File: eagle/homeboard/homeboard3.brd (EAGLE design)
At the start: 100 x 80 mm, 81 parts, among them IC1 XCF02S, IC2 25LC080SN, Q5 BC848SMD, Q6 BC848SMD, Q7 BC848SMD, Q8 BC848SMD, T1 BSS138, T2 BC848, T3 BSS138, U1 XC3S400TQ144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

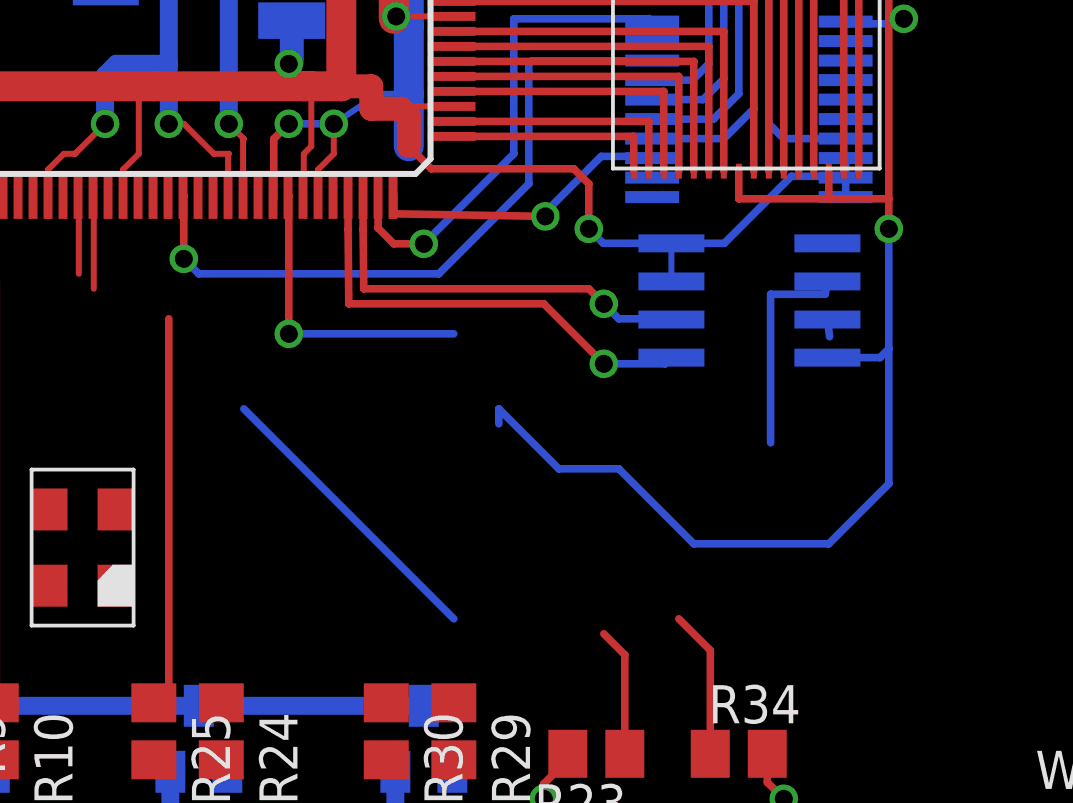
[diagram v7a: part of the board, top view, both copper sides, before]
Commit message: wired up prog and flash
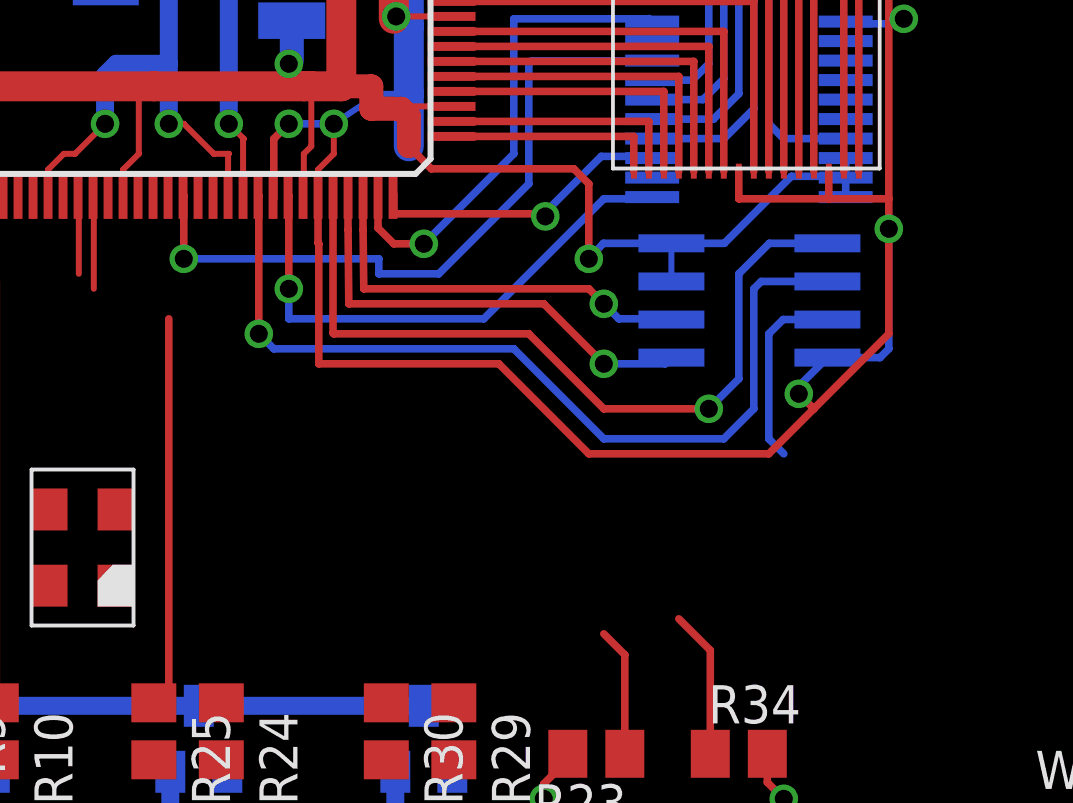
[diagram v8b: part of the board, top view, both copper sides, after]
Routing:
- net SPI_SEL0: track 0.00 -> 26.5 mm, vias 0 -> 1
- net GND: track 271.5 -> 284.2 mm, vias 20 -> 21
- net MISO: track 17.1 -> 29.6 mm, vias 0 -> 1
- net PROM_DO: track 10.2 -> 17.9 mm
- net N$49: track 0.58 -> 6.36 mm
- net VCC: track 221.5 -> 222.6 mm
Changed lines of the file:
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@@
 <wire x1="51" y1="16.1" x2="50.35" y2="16.75" width="0.254" layer="16"/>
 <wire x1="50.35" y1="16.75" x2="53.65" y2="16.75" width="0.254" layer="16"/>
-<wire x1="59.5" y1="33.5" x2="59.5" y2="29" width="0.254" layer="16"/>
-<wire x1="59.5" y1="29" x2="57.5" y2="27" width="0.254" layer="16"/>
-<wire x1="57.5" y1="27" x2="53" y2="27" width="0.254" layer="16"/>
-<wire x1="53" y1="27" x2="50.5" y2="29.5" width="0.254" layer="16"/>
-<wire x1="50.5" y1="29.5" x2="48.5" y2="29.5" width="0.254" layer="16"/>
-<wire x1="48.5" y1="29.5" x2="46.5" y2="31.5" width="0.254" layer="16"/>
-<wire x1="46.5" y1="31.5" x2="46.5" y2="31" width="0.254" layer="16"/>
+<wire x1="40.475" y1="38.63" x2="40.475" y2="37.025" width="0.254" layer="1"/>
+<wire x1="40.475" y1="37.025" x2="40.5" y2="37" width="0.254" layer="1"/>
+<wire x1="40.5" y1="37" x2="40.5" y2="33" width="0.254" layer="1"/>
+<wire x1="40.5" y1="33" x2="46.5" y2="33" width="0.254" layer="1"/>
+<wire x1="46.5" y1="33" x2="49.5" y2="30" width="0.254" layer="1"/>
+<via x="56.5" y="32" extent="1-16" drill="0.6" shape="square"/>
+<wire x1="56.5" y1="32" x2="56.5" y2="32.252359375" width="0.254" layer="16"/>
+<wire x1="56.5" y1="32.252359375" x2="57.453553125" y2="33.2059125" width="0.254" layer="16"/>
+<wire x1="49.5" y1="30" x2="55.5" y2="30" width="0.254" layer="1"/>
+<wire x1="55.5" y1="30" x2="57" y2="31.5" width="0.254" layer="1"/>
+<wire x1="57" y1="31.5" x2="59.5" y2="34" width="0.254" layer="1"/>
+<wire x1="59.5" y1="34" x2="59.5" y2="37.5" width="0.254" layer="1"/>
+<wire x1="56.5" y1="32" x2="57" y2="31.5" width="0.254" layer="1"/>
 <wire x1="96.05" y1="71" x2="95.55" y2="76" width="0" layer="19" extent="1-1"/>
 <wire x1="96.55" y1="67.5" x2="96.05" y2="71" width="0" layer="19" extent="1-1"/>
@@
 <wire x1="38.975" y1="38.63" x2="39" y2="38.5" width="0" layer="19" extent="1-1"/>
 <wire x1="29.475" y1="38.63" x2="28" y2="38.655" width="0" layer="19" extent="1-1"/>
-<wire x1="46.5" y1="31.5" x2="43.5" y2="40.25" width="0" layer="19" extent="16-16"/>
-<wire x1="53.65" y1="16.75" x2="53" y2="27" width="0" layer="19" extent="16-16"/>
+<wire x1="33.725" y1="28.145" x2="40.5" y2="33" width="0" layer="19" extent="1-1"/>
+<wire x1="50.35" y1="16.75" x2="49.5" y2="30" width="0" layer="19" extent="1-16"/>
 <wire x1="46.335" y1="7.5" x2="46.5" y2="7.5" width="0" layer="19" extent="1-1"/>
 <wire x1="19.665" y1="7.5" x2="19.5" y2="7.5" width="0" layer="19" extent="1-1"/>
 <wire x1="21.5" y1="4.93" x2="19.5" y2="5" width="0" layer="19" extent="1-1"/>
-<wire x1="33.725" y1="28.145" x2="29.475" y2="38.63" width="0" layer="19" extent="1-1"/>
-<wire x1="70.77" y1="21.75" x2="59.5" y2="29" width="0" layer="19" extent="16-16"/>
+<wire x1="70.77" y1="21.75" x2="59.2059125" y2="33.2059125" width="0" layer="19" extent="16-16"/>
 <wire x1="70.77" y1="18" x2="70.77" y2="21.75" width="0" layer="19" extent="1-1"/>
 <wire x1="17.3716" y1="78.27" x2="34.9778" y2="77" width="0" layer="19" extent="1-1"/>
@@
 <wire x1="58.043396875" y1="39.206603125" x2="58" y2="39.25" width="0.254" layer="16"/>
 <wire x1="52.253553125" y1="37.0159125" x2="49.9840875" y2="37.0159125" width="0.254" layer="16"/>
-<wire x1="49.9840875" y1="37.0159125" x2="49.5" y2="37.5" width="0.254" layer="16"/>
-<via x="49.5" y="37.5" extent="1-16" drill="0.6" shape="square"/>
-<wire x1="49.5" y1="37.5" x2="49.5" y2="39" width="0.254" layer="1"/>
+<wire x1="49.9840875" y1="37.0159125" x2="49.5" y2="36.5" width="0.254" layer="16"/>
+<via x="49.5" y="36.5" extent="1-16" drill="0.6" shape="square"/>
+<wire x1="49.5" y1="36.5" x2="49.5" y2="39" width="0.254" layer="1"/>
 <wire x1="49.5" y1="39" x2="49" y2="39.5" width="0.254" layer="1"/>
 <wire x1="49" y1="39.5" x2="44.25" y2="39.5" width="0.254" layer="1"/>
@@
 <wire x1="47.5" y1="43" x2="47.5" y2="39" width="0.254" layer="16"/>
 <wire x1="47.5" y1="39" x2="44.5" y2="36" width="0.254" layer="16"/>
-<wire x1="44.5" y1="36" x2="36.5" y2="36" width="0.254" layer="16"/>
-<wire x1="36.5" y1="36" x2="36" y2="36.5" width="0.254" layer="16"/>
+<wire x1="44.5" y1="36" x2="42.5" y2="36" width="0.254" layer="16"/>
+<wire x1="42.5" y1="36" x2="42.5" y2="36.5" width="0.254" layer="16"/>
+<wire x1="42.5" y1="36.5" x2="36" y2="36.5" width="0.254" layer="16"/>
 </signal>
 <signal name="N$39">
@@
 <wire x1="51.612590625" y1="39.856603125" x2="51.55498125" y2="39.9142125" width="0.254" layer="16"/>
 <wire x1="43" y1="38.655" x2="43" y2="38" width="0.254" layer="1"/>
-<wire x1="43" y1="38" x2="48.05025" y2="37.9142125" width="0.254" layer="1"/>
 <wire x1="51.55498125" y1="39.9142125" x2="49.9142125" y2="39.9142125" width="0.254" layer="16"/>
 <wire x1="49.9142125" y1="39.9142125" x2="48" y2="38" width="0.254" layer="16"/>
 <wire x1="48" y1="38" x2="48" y2="37.9644625" width="0.254" layer="16"/>
 <wire x1="48" y1="37.9644625" x2="48.05025" y2="37.9142125" width="0.254" layer="16"/>
+<wire x1="43" y1="38" x2="48" y2="38" width="0.254" layer="1"/>
+<wire x1="48.05025" y1="37.9142125" x2="48.05025" y2="37.94975" width="0.254" layer="1"/>
+<wire x1="48.05025" y1="37.94975" x2="48" y2="38" width="0.254" layer="1"/>
 </signal>
 <signal name="N$38">
@@
 <contactref element="U1" pad="P65"/>
 <wire x1="51.612590625" y1="38.556603125" x2="51.555984375" y2="38.5" width="0.254" layer="16"/>
-<via x="39.5" y="34" extent="1-16" drill="0.6" shape="square"/>
-<wire x1="39.5" y1="34" x2="39.5" y2="38.605" width="0.254" layer="1"/>
+<via x="39.5" y="35.5" extent="1-16" drill="0.6" shape="square"/>
+<wire x1="39.5" y1="35.5" x2="39.5" y2="38.605" width="0.254" layer="1"/>
 <wire x1="39.5" y1="38.605" x2="39.475" y2="38.63" width="0.254" layer="1"/>
-<wire x1="45" y1="34" x2="39.5" y2="34" width="0.254" layer="16"/>
-<wire x1="45" y1="34" x2="51.555984375" y2="38.5" width="0" layer="19" extent="16-16"/>
+<wire x1="51.555984375" y1="38.5" x2="50" y2="38.5" width="0.254" layer="16"/>
+<wire x1="50" y1="38.5" x2="46" y2="34.5" width="0.254" layer="16"/>
+<wire x1="46" y1="34.5" x2="39.5" y2="34.5" width="0.254" layer="16"/>
+<wire x1="39.5" y1="34.5" x2="39.5" y2="35.5" width="0.254" layer="16"/>
 </signal>
 <signal name="VCCINT">
@@
 <contactref element="IC2" pad="2"/>
 <contactref element="U$3" pad="11"/>
-<wire x1="57.453553125" y1="35.7459125" x2="57.381446875" y2="35.31801875" width="0.254" layer="16"/>
-<wire x1="57.381446875" y1="35.31801875" x2="55.560659375" y2="35.31801875" width="0.254" layer="16"/>
-<wire x1="55.560659375" y1="35.31801875" x2="55.560659375" y2="30.368271875" width="0.254" layer="16"/>
-<wire x1="45" y1="24.5" x2="38" y2="31.5" width="0.254" layer="16"/>
 <contactref element="U1" pad="P63"/>
+<wire x1="54" y1="30.5" x2="50" y2="30.5" width="0.254" layer="16"/>
+<wire x1="50" y1="30.5" x2="47" y2="33.5" width="0.254" layer="16"/>
+<wire x1="47" y1="33.5" x2="39" y2="33.5" width="0.254" layer="16"/>
+<wire x1="39" y1="33.5" x2="38.5" y2="34" width="0.254" layer="16"/>
+<via x="38.5" y="34" extent="1-16" drill="0.6" shape="square"/>
+<wire x1="38.5" y1="34" x2="38.5" y2="38.605" width="0.254" layer="1"/>
+<wire x1="38.5" y1="38.605" x2="38.475" y2="38.63" width="0.254" layer="1"/>
+<wire x1="54" y1="30.5" x2="55" y2="31.5" width="0.254" layer="16"/>
+<wire x1="57.453553125" y1="35.7459125" x2="55.2459125" y2="35.7459125" width="0.254" layer="16"/>
+<wire x1="55.2459125" y1="35.7459125" x2="55" y2="35.5" width="0.254" layer="16"/>
+<wire x1="55" y1="35.5" x2="55" y2="31.5" width="0.254" layer="16"/>
 <wire x1="57.453553125" y1="35.7459125" x2="87.2" y2="63.5" width="0" layer="19" extent="16-16"/>
-<wire x1="45" y1="24.5" x2="55.560659375" y2="30.368271875" width="0" layer="19" extent="16-16"/>
-<wire x1="38.475" y1="38.63" x2="38" y2="31.5" width="0" layer="19" extent="1-16"/>
 </signal>
 <signal name="SPI_SEL0">
 <contactref element="IC2" pad="1"/>
 <contactref element="U1" pad="P68"/>
-<wire x1="40.975" y1="38.63" x2="57.453553125" y2="37.0159125" width="0" layer="19" extent="1-16"/>
+<wire x1="57.453553125" y1="37.0159125" x2="55.5159125" y2="37.0159125" width="0.254" layer="16"/>
+<wire x1="55.5159125" y1="37.0159125" x2="54.5" y2="36" width="0.254" layer="16"/>
+<wire x1="54.5" y1="36" x2="54.5" y2="32.5" width="0.254" layer="16"/>
+<wire x1="40.975" y1="38.63" x2="40.975" y2="34.025" width="0.254" layer="1"/>
+<wire x1="40.975" y1="34.025" x2="41" y2="34" width="0.254" layer="1"/>
+<wire x1="41" y1="34" x2="47.5" y2="34" width="0.254" layer="1"/>
+<wire x1="47.5" y1="34" x2="50" y2="31.5" width="0.254" layer="1"/>
+<wire x1="50" y1="31.5" x2="53.5" y2="31.5" width="0.254" layer="1"/>
+<via x="53.5" y="31.5" extent="1-16" drill="0.6" shape="square"/>
+<wire x1="53.5" y1="31.5" x2="54.5" y2="32.5" width="0.254" layer="16"/>
 </signal>
 <signal name="N$49">
@@
 <contactref element="R47" pad="1"/>
 <contactref element="WR_PROT" pad="2"/>
-<wire x1="57.453553125" y1="34.4759125" x2="57.525659375" y2="33.903803125" width="0.254" layer="16"/>
+<wire x1="57.453553125" y1="34.4759125" x2="55.9759125" y2="34.4759125" width="0.254" layer="16"/>
+<wire x1="55.9759125" y1="34.4759125" x2="55.5" y2="34" width="0.254" layer="16"/>
+<wire x1="55.5" y1="34" x2="55.5" y2="30.5" width="0.254" layer="16"/>
+<wire x1="55.5" y1="30.5" x2="56" y2="30" width="0.254" layer="16"/>
 <wire x1="68.23" y1="21.75" x2="75.55" y2="27.5" width="0" layer="19" extent="16-16"/>
-<wire x1="57.525659375" y1="33.903803125" x2="68.23" y2="21.75" width="0" layer="19" extent="16-16"/>
+<wire x1="56" y1="30" x2="68.23" y2="21.75" width="0" layer="19" extent="16-16"/>
 </signal>
 <signal name="N$50">
